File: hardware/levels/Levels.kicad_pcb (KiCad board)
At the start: 2 copper layers, 15 x 100 mm, 7 parts, among them J1 AudioJack2_SwitchT, J2 AudioJack2_SwitchT, J3 AudioJack2_SwitchT, J4 AudioJack2_SwitchT

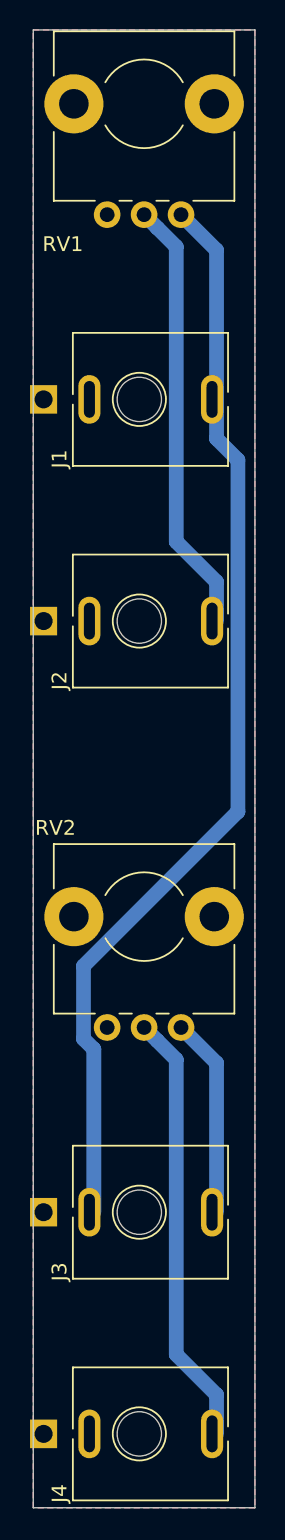
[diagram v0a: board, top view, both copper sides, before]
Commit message: Center jacks on PCB
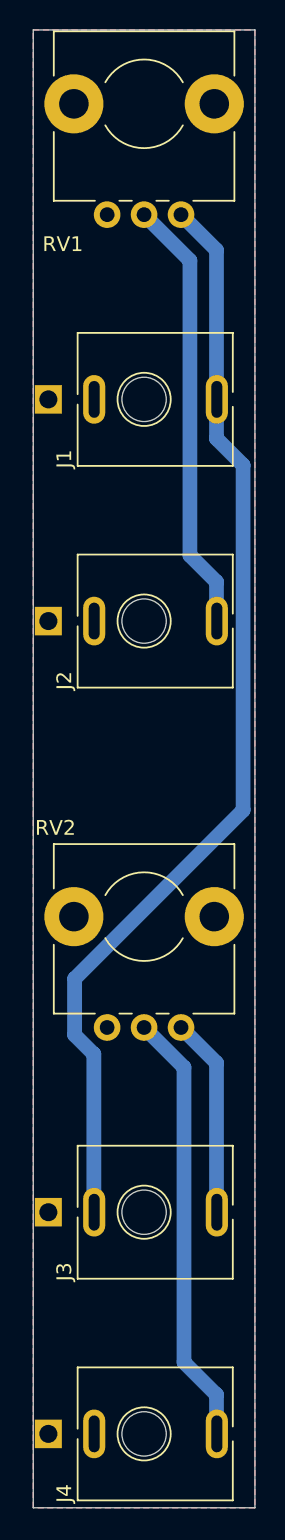
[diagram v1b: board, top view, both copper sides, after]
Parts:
- moved J1 0.32 mm to (151.0, 75.0)
- moved J2 0.32 mm to (151.0, 90.0)
- moved J3 0.32 mm to (151.0, 130.0)
- moved J4 0.32 mm to (151.0, 145.0)
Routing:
- net Net-(J1-PadT): track 73.7 -> 74.5 mm
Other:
- board text added: "ST-02 v1.1 Levels"
- board text removed: "ST-02 v1.0 Levels"
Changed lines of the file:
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@@
 		(title "Levels")
 		(date "2026-10-07")
-		(rev "1.0")
+		(rev "1.1")
 		(company "Schenktronics")
 		(comment 4 "PCB-ST02-MAIN")
@@
 	(footprint "_NTSFootprints:Jack_3.5mm_QingPu_WQP-PJ398SM_Vertical_CenterHole_OvalPads"
 		(layer "F.Cu")
-		(at 150.7 90 90)
+		(at 151.023 90 90)
 		(descr "TRS 3.5mm, vertical, Thonkiconn, PCB mount, (http://www.qingpu-electronics.com/en/products/WQP-PJ398SM-362.html)")
 		(tags "WQP-PJ398SM WQP-PJ301M-12 TRS 3.5mm mono vertical jack thonkiconn qingpu")
@@
 	(footprint "_NTSFootprints:Jack_3.5mm_QingPu_WQP-PJ398SM_Vertical_CenterHole_OvalPads"
 		(layer "F.Cu")
-		(at 150.7 145 90)
+		(at 151.023 145 90)
 		(descr "TRS 3.5mm, vertical, Thonkiconn, PCB mount, (http://www.qingpu-electronics.com/en/products/WQP-PJ398SM-362.html)")
 		(tags "WQP-PJ398SM WQP-PJ301M-12 TRS 3.5mm mono vertical jack thonkiconn qingpu")
@@
 	(footprint "_NTSFootprints:Jack_3.5mm_QingPu_WQP-PJ398SM_Vertical_CenterHole_OvalPads"
 		(layer "F.Cu")
-		(at 150.7 130 90)
+		(at 151.023 130 90)
 		(descr "TRS 3.5mm, vertical, Thonkiconn, PCB mount, (http://www.qingpu-electronics.com/en/products/WQP-PJ398SM-362.html)")
 		(tags "WQP-PJ398SM WQP-PJ301M-12 TRS 3.5mm mono vertical jack thonkiconn qingpu")
@@
 	(footprint "_NTSFootprints:Jack_3.5mm_QingPu_WQP-PJ398SM_Vertical_CenterHole_OvalPads"
 		(layer "F.Cu")
-		(at 150.7 75 90)
+		(at 151.023 75 90)
 		(descr "TRS 3.5mm, vertical, Thonkiconn, PCB mount, (http://www.qingpu-electronics.com/en/products/WQP-PJ398SM-362.html)")
 		(tags "WQP-PJ398SM WQP-PJ301M-12 TRS 3.5mm mono vertical jack thonkiconn qingpu")
@@
 		)
 	)
-	(gr_text "ST-02 v1.0\nLevels"
+	(gr_text "ST-02 v1.1\nLevels"
 		(at 157.5 94.8 0)
 		(layer "B.SilkS")
@@
 	)
 	(segment
-		(start 159.677001 64.677001)
-		(end 158.399999 63.399999)
-		(width 1)
-		(layer "B.Cu")
-		(net "Net-(J2-PadT)")
-	)
-	(segment
-		(start 158.399999 63.399999)
-		(end 157.5 62.5)
-		(width 1)
-		(layer "B.Cu")
-		(net "Net-(J2-PadT)")
-	)
-	(segment
 		(start 162.4 90)
 		(end 162.4 87.35)
@@
 	)
 	(segment
-		(start 162.4 87.35)
-		(end 159.677001 84.627001)
+		(start 160.6 85.55)
+		(end 160.6 65.6)
 		(width 1)
 		(layer "B.Cu")
@@
 	)
 	(segment
-		(start 159.677001 84.627001)
-		(end 159.677001 64.677001)
+		(start 160.6 65.6)
+		(end 157.5 62.5)
 		(width 1)
 		(layer "B.Cu")
@@
 	)
 	(segment
-		(start 163.85001 102.895992)
-		(end 163.85001 79.10001)
+		(start 162.4 87.35)
+		(end 160.6 85.55)
 		(width 1)
 		(layer "B.Cu")
-		(net "Net-(J1-PadT)")
+		(net "Net-(J2-PadT)")
 	)
 	(segment
-		(start 154.1 130)
-		(end 154.1 118.968002)
-		(width 1)
-		(layer "B.Cu")
-		(net "Net-(J1-PadT)")
-	)
-	(segment
-		(start 153.399999 113.346003)
-		(end 163.85001 102.895992)
-		(width 1)
-		(layer "B.Cu")
-		(net "Net-(J1-PadT)")
-	)
-	(segment
-		(start 163.85001 79.10001)
+		(start 164.2 79.45)
 		(end 162.4 77.65)
 		(width 1)
@@
 	)
 	(segment
-		(start 162.4 75)
-		(end 162.4 64.9)
+		(start 152.8 114.2)
+		(end 164.2 102.8)
 		(width 1)
 		(layer "B.Cu")
@@
 	)
 	(segment
-		(start 154.1 118.968002)
-		(end 153.399999 118.268001)
+		(start 154.1 119.300001)
+		(end 152.8 118.000001)
+		(width 1)
+		(layer "B.Cu")
+		(net "Net-(J1-PadT)")
+	)
+	(segment
+		(start 164.2 102.8)
+		(end 164.2 79.45)
 		(width 1)
 		(layer "B.Cu")
@@
 	)
 	(segment
-		(start 153.399999 118.268001)
-		(end 153.399999 113.346003)
+		(start 154.1 130)
+		(end 154.1 119.300001)
 		(width 1)
 		(layer "B.Cu")
@@
 	)
 	(segment
-		(start 162.4 77.65)
-		(end 162.4 75)
+		(start 152.8 118.000001)
+		(end 152.8 114.2)
 		(width 1)
 		(layer "B.Cu")
@@
 	)
 	(segment
-		(start 159.677001 119.677001)
-		(end 158.399999 118.399999)
+		(start 162.4 77.65)
+		(end 162.4 64.9)
+		(width 1)
+		(layer "B.Cu")
+		(net "Net-(J1-PadT)")
+	)
+	(segment
+		(start 162.4 142.35)
+		(end 160.2 140.15)
 		(width 1)
 		(layer "B.Cu")
@@
 	)
 	(segment
-		(start 159.677001 139.627001)
-		(end 159.677001 119.677001)
-		(width 1)
-		(layer "B.Cu")
-		(net "Net-(J4-PadT)")
-	)
-	(segment
-		(start 162.4 142.35)
-		(end 159.677001 139.627001)
-		(width 1)
-		(layer "B.Cu")
-		(net "Net-(J4-PadT)")
-	)
-	(segment
-		(start 158.399999 118.399999)
-		(end 157.5 117.5)
+		(start 160.2 140.15)
+		(end 160.2 120.2)
 		(width 1)
 		(layer "B.Cu")
@@
 		(width 1)
 		(layer "B.Cu")
+		(net "Net-(J4-PadT)")
+	)
+	(segment
+		(start 160.2 120.2)
+		(end 157.5 117.5)
+		(width 1)
+		(layer "B.Cu")
